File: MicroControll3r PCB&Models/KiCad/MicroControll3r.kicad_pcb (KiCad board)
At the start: 2 copper layers, 69.8 x 86.8 mm, 9 parts, among them SW1 SW_Push, SW2 SW_Push, SW3 SW_Push, SW4 SW_Push, U1 XIAO-RP2040-DIP

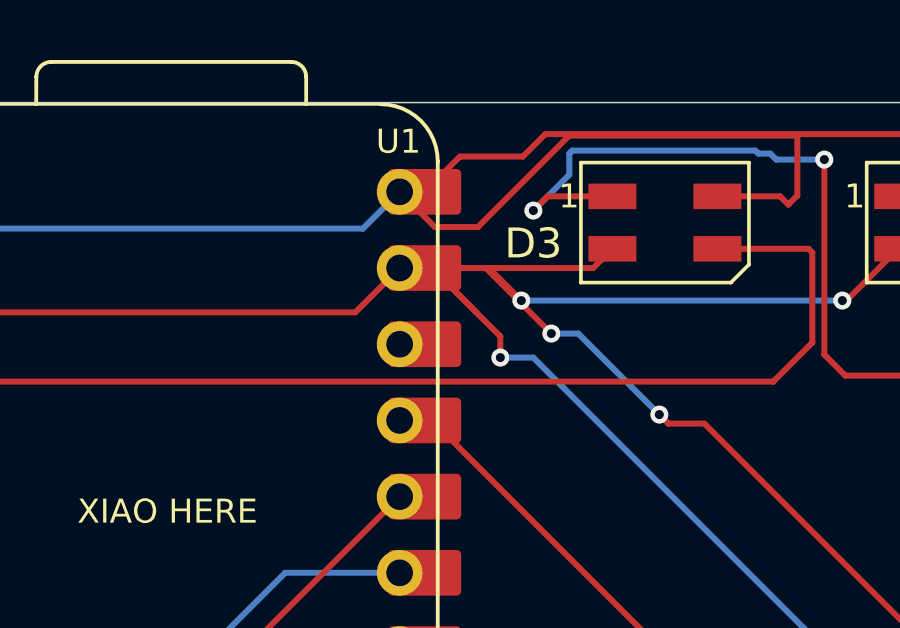
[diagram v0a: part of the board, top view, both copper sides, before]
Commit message: Updated PCB models
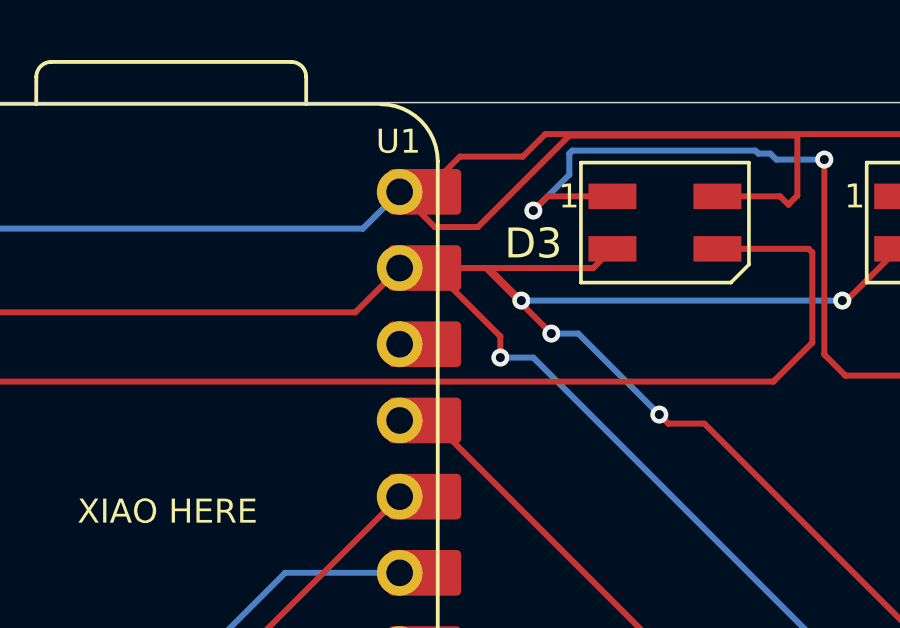
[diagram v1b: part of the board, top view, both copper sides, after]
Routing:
- net GND: track 280.8 -> 278.7 mm
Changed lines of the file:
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@@
 			(outputformat 1)
 			(mirror no)
-			(drillshape 1)
+			(drillshape 0)
 			(scaleselection 1)
-			(outputdirectory "")
+			(outputdirectory "C:/Users/PC/Downloads/")
 		)
 	)
@@
 	)
 	(segment
+		(start 201 59.5)
+		(end 201 58.79362)
+		(width 0.2)
+		(layer "F.Cu")
+		(net 2)
+	)
+	(segment
 		(start 194.5 114.1)
 		(end 197 114.1)
@@
 	)
 	(segment
-		(start 197.64375 56.515)
-		(end 198.72138 56.515)
-		(width 0.2)
-		(layer "F.Cu")
-		(net 2)
-	)
-	(segment
 		(start 166.1 58.5)
 		(end 170.8 58.5)
@@
 	)
 	(segment
-		(start 201 59.4)
-		(end 201 59.5)
-		(width 0.2)
-		(layer "F.Cu")
-		(net 2)
-	)
-	(segment
 		(start 193.1 98.9)
 		(end 192.3575 99.6425)
@@
 	(segment
 		(start 201 58.79362)
-		(end 201 59.4)
+		(end 198.72138 56.515)
 		(width 0.2)
 		(layer "F.Cu")
@@
 	)
 	(segment
-		(start 198.72138 56.515)
-		(end 200.2 57.99362)
-		(width 0.2)
-		(layer "F.Cu")
-		(net 2)
-	)
-	(segment
 		(start 190.2 118.46875)
 		(end 192.3575 120.62625)
@@
 	)
 	(segment
-		(start 198.72138 56.515)
-		(end 201 58.79362)
-		(width 0.2)
-		(layer "F.Cu")
-		(net 2)
-	)
-	(segment
 		(start 192.3575 116.2425)
 		(end 194.5 114.1)
@@
 		(width 0.2)
 		(layer "F.Cu")
+		(net 2)
+	)
+	(segment
+		(start 198.72138 56.515)
+		(end 197.64375 56.515)
+		(width 0.2)
+		(layer "F.Cu")
